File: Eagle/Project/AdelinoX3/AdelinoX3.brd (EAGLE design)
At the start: 47 x 53.3 mm, 80 parts, among them J1 DC-044-A, J2 YELLOW-8P-2.54, J3 YELLOW-6P-2.54, J4 YELLOW-8P-2.54, J5 YELLOW-8P-2.54, J6 4P-2.0, J7 YELLOW-2X3P-2.54, J8 4P-2.0, Q1 NCE3407A, Q2 CJ2305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

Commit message: Wip; use same parts as Seeeduino for SPS.
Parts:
- added L3, L4: 470R-2A, OPL_Ferrite_and_Magnetic_Bead:L0805
- added R30: 24K, Seeed-Resistor:R0603
- C2, C3: value 10uf -> 22uf; device Seeed-Capacitor:C0805 -> Seeed-Capacitor:C1206
- R1: value 100K 1/10W -> 100K
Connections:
- removed net SW_EN: R1.1, U2.6
- new net N$7: R1.2, R30.2, U2.6
- new net N$8: L3.1, Q1.2
- net GND: now also R30.1
- net SW_VCC_IN: now also L3.2, R1.1; no longer Q1.2, R1.2
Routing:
- net SW_EN: track 10.5 -> 0.00 mm, vias 2 -> 0
- net SW_VCC_IN: track 7.67 -> 3.56 mm

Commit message: Schematic changes to 0603 done.
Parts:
- added C22, C23: 10uf, Seeed-Capacitor:C0805
- added C24: 22uf, Seeed-Capacitor:C1206
- C6: value 10uf -> 22uf; device Seeed-Capacitor:C0805 -> OPL_Capacitor:C1206
- R28, R5: device Seeed-Resistor:R0402 -> Seeed-Resistor:R0603
- R4: value 10R 1/16W -> 10R; device Seeed-Resistor:R0402 -> Seeed-Resistor:R0603
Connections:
- new net N$10: C10.2, C22.2, C9.2, L2.2, L4.1, R7.2
- net +5V: now also C23.2, C24.2, L4.2; no longer C10.2, C9.2, L2.2, R7.2
- net GND: now also C22.1, C23.1, C24.1
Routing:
- net +5V: track 219.4 -> 208.7 mm
- net N$10: track 0.00 -> 9.04 mm
- net +3V3: track 111.6 -> 113.2 mm

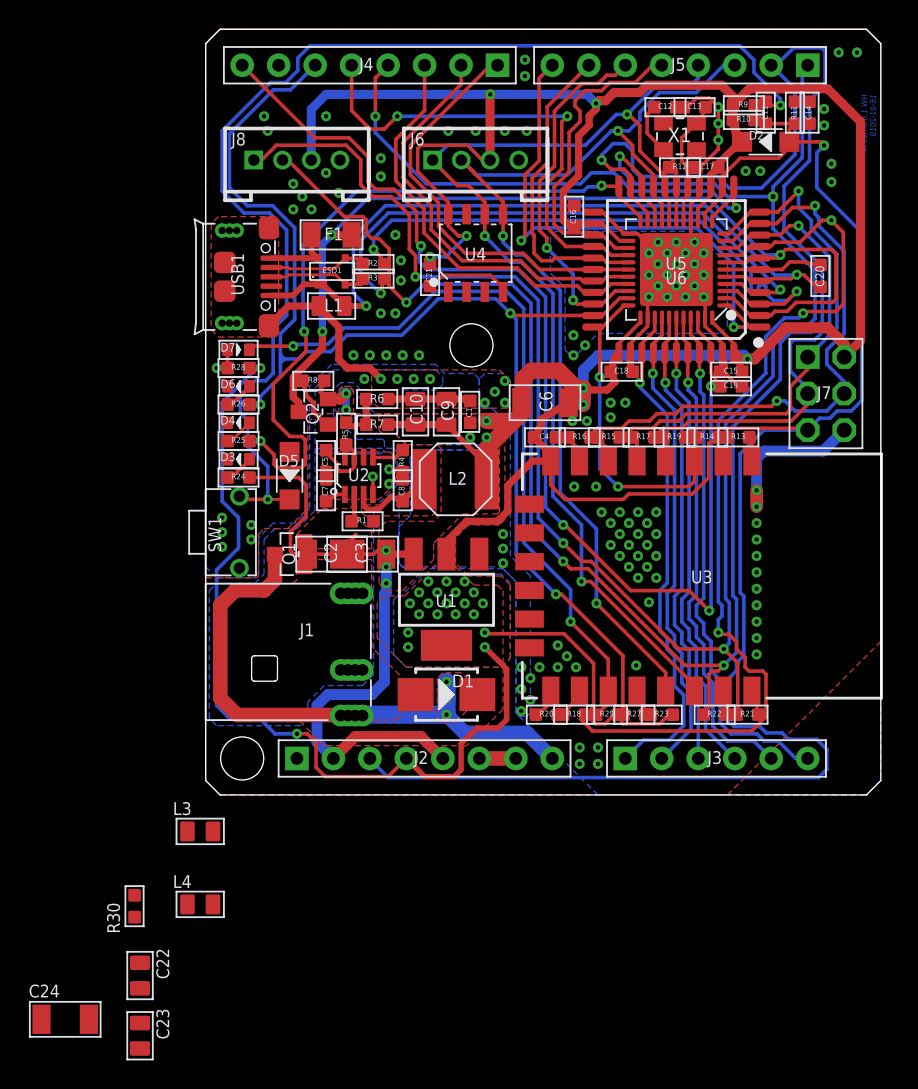
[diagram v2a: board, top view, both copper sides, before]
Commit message: First X3 routing finished.
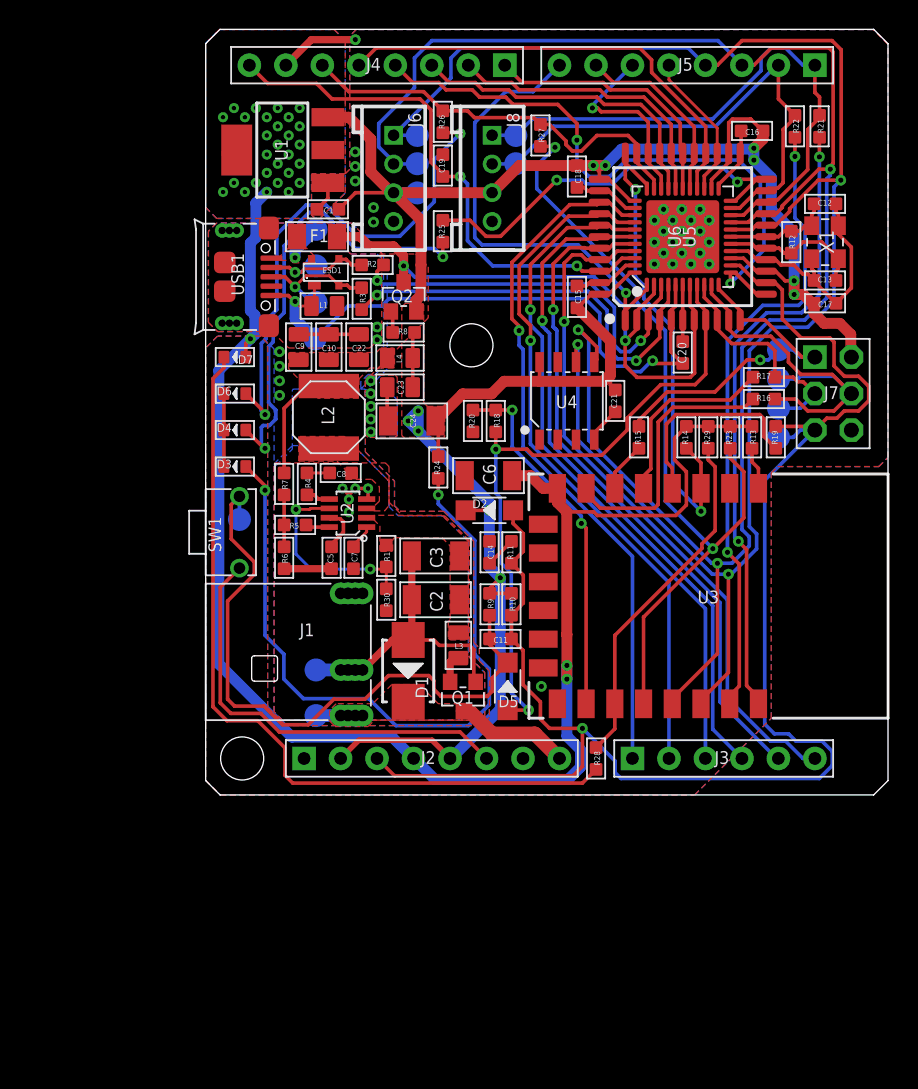
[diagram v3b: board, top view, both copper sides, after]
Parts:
- removed C4: 100nf, OPL_Capacitor:C0603
- added TP1, TP10, TP11, TP12, TP13, TP14, TP15, TP16, TP17, TP2, TP3, TP4, TP5, TP6, TP7, TP8, TP9: TPTP16R, testpad:TP16R
- R10, R20, R8, R9: value 100K 1/10W -> 100K
- R11, R13, R14, R23, R29: value 10K 1/10W -> 10K
- R12: value 1M 1/10W -> 1M
- R15, R16, R17, R21, R22, R24, R25, R26, R27: value 1K 1/10W -> 1K
- U1: value CJT1117-3.3-SOT223 -> CJT1117-3.3
- U3: device Seeed-OPL-2017-01-Sensor-camilo:ESP-12F -> Adelino-Misc:ESP-12F
- moved C23 48.6 mm to (13.5, 28.4), turned to 90 degrees
- moved C24 48.1 mm to (14.4, 26.0)
- moved C22 46.3 mm to (10.7, 31.2)
- moved R22 41.3 mm to (41.0, 46.5), turned to 180 degrees
- moved R21 41.3 mm to (42.7, 46.5), turned to 180 degrees
- moved C11 41.0 mm to (20.5, 10.9), turned to 270 degrees
- moved R27 40.8 mm to (23.3, 45.9), turned to 0 degrees
- moved L4 40.5 mm to (13.5, 30.4)
- moved R9 39.0 mm to (19.8, 13.3), turned to 0 degrees
- moved C14 37.9 mm to (19.8, 16.9), turned to 180 degrees
- moved R10 37.4 mm to (21.3, 13.3), turned to 180 degrees
- moved R28 36.9 mm to (27.2, 2.54), turned to 180 degrees
- moved R11 36.4 mm to (21.3, 16.9)
- moved U1 33.3 mm to (5.33, 44.9), turned to 90 degrees
- moved D2 32.1 mm to (19.7, 19.8)
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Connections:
- net N$10 renamed SW_F1
- net N$12 renamed GPIO12
- net N$14 renamed GPIO13
- net N$17 renamed TXD
- net N$18 renamed RXD
- net N$19 renamed GPIO14
- net N$20 renamed GPIO15
- net N$22 renamed RST
- net N$5 renamed GPIO16
- net N$6 renamed _ACT
- removed net N$1: ESD1.3, R2.1, USB1.2
- removed net N$2: ESD1.2, R3.1, USB1.3
- removed net N$4: D7.+, R28.2
- removed net N$9: ESD1.4, F1.1, USB1.1
- new net UD+: ESD1.2, R3.1, TP7.TP, USB1.3
- new net UD-: ESD1.3, R2.1, TP6.TP, USB1.2
- new net UVCC: ESD1.4, F1.1, TP5.TP, USB1.1
- new net _ESP: D7.-, R28.1
- net +3V3: now also D7.+, TP16.TP; no longer C4.2, R28.1
- net +5V: now also TP17.TP
- net AT_MISO: now also TP1.TP
- net AT_MOSI: now also TP4.TP
- net AT_SCK: now also TP2.TP
- net GND: now also TP10.TP; no longer C4.1
- net GPIO2_LED: now also R28.2; no longer D7.-
- net PIN_D0: now also TP12.TP
- net PIN_D1: now also TP13.TP
- net PIN_D2_SDA: now also TP14.TP
- net PIN_D3_SCL: now also TP15.TP
- net RESET: now also TP3.TP
- net RSTAT: now also TP11.TP
- net UGND: now also TP8.TP
- net VIN: now also TP9.TP
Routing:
- net PIN_D1: track 145.3 -> 36.1 mm, vias 4 -> 0
- net PIN_D0: track 129.5 -> 40.4 mm, vias 5 -> 0
- net PIN_D13: track 90.6 -> 28.8 mm, vias 3 -> 0
- net _ESP: track 0.00 -> 55.0 mm
- net BOOT_MODE: track 2.18 -> 55.7 mm, vias 0 -> 2
- net PIN_D2_SDA: track 73.7 -> 125.9 mm
- net _PWR: track 2.05 -> 49.4 mm, vias 0 -> 2
- net PIN_D3_SCL: track 76.2 -> 120.6 mm
- net +5V: track 208.7 -> 164.7 mm, vias 15 -> 11
- net PIN_AREF: track 81.5 -> 37.7 mm, vias 4 -> 2
- net RXD: track 1.73 -> 44.1 mm, vias 0 -> 2
- net TXD: track 1.75 -> 44.0 mm, vias 0 -> 2
- net RSTAT: track 81.2 -> 45.3 mm, vias 2 -> 0
- net GND: track 76.8 -> 111.2 mm, vias 137 -> 44
- net _D13: track 2.05 -> 35.5 mm, vias 0 -> 2
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- added copper zone on layer 1, net SW_F1
- added copper zone on layer 1, net UVCC
- removed copper zone on layer 16, net +5V
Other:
- board size 47 x 53.3 mm -> 47.5 x 53.3 mm
- board text added: "PWR"
- board text removed: "ECC 608"
- board text removed: "HW 1.0.0 Rev A 16-01-2019"
- board text removed: "I2C"
- board text removed: "ON"
- board text removed: "UART"

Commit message: Routing review in progress.
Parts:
- moved R18 1.65 mm to (18.5, 26.0)
- moved R20 1.46 mm to (20.1, 26.0)
- moved C23 0.13 mm to (13.7, 28.4)
- moved L4 0.13 mm to (13.7, 30.4)
- moved C24 0.13 mm to (14.5, 26.0)
- moved Q2 0.13 mm to (13.9, 34.7)
- moved R8 0.13 mm to (13.9, 32.2)
- moved C22 0.06 mm to (10.6, 31.2)
- moved C9 0.06 mm to (6.54, 31.2)
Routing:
- net AT_SS: track 45.9 -> 48.2 mm
- net +5V: track 164.7 -> 166.6 mm, vias 11 -> 10
- net N$8: track 1.76 -> 0.00 mm
- net GPIO15: track 25.3 -> 24.1 mm
- net UGND: track 44.6 -> 45.6 mm
- net D+: track 29.4 -> 30.4 mm
- net SW_VCC_OUT: track 0.92 -> 0.00 mm
- net D-: track 28.0 -> 28.8 mm
- net SW_VCC_IN: track 0.64 -> 0.00 mm
- net VUSB: track 44.0 -> 44.6 mm
- added copper zone on layer 1, net N$8

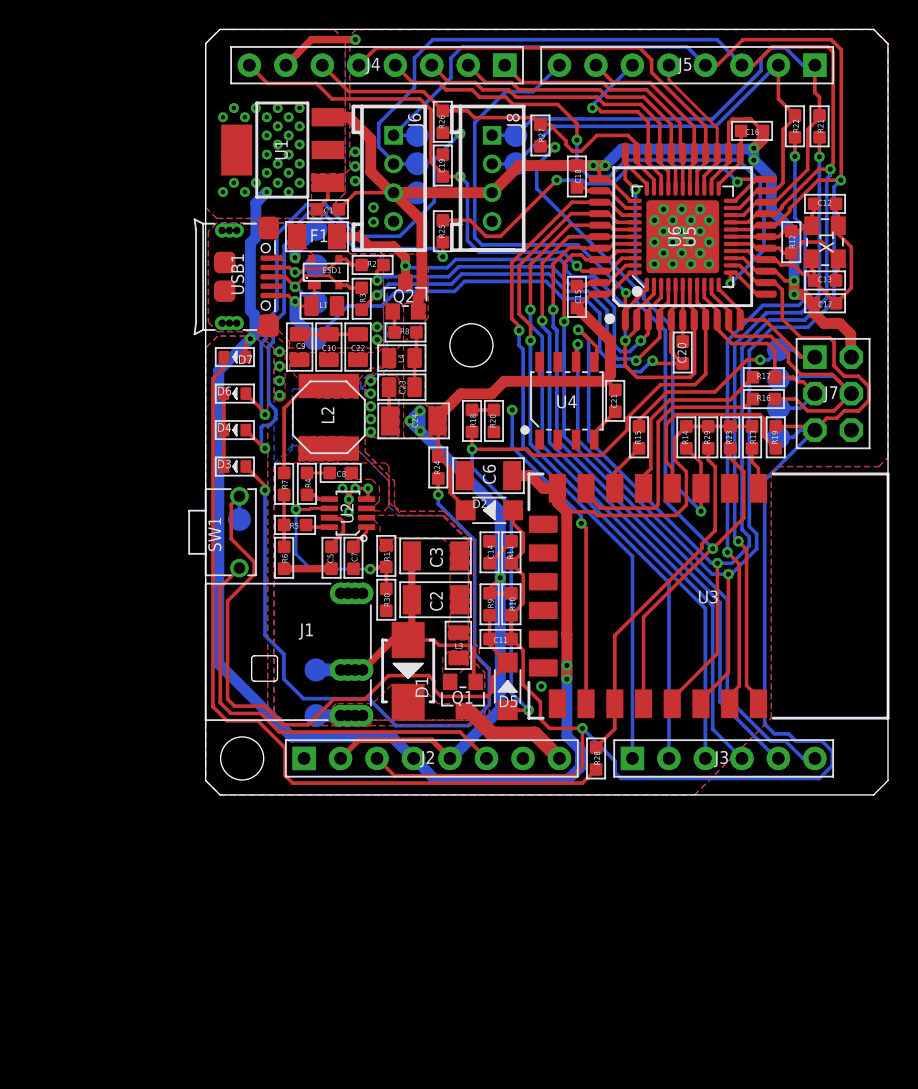
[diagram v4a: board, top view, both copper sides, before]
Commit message: Routing review finished.
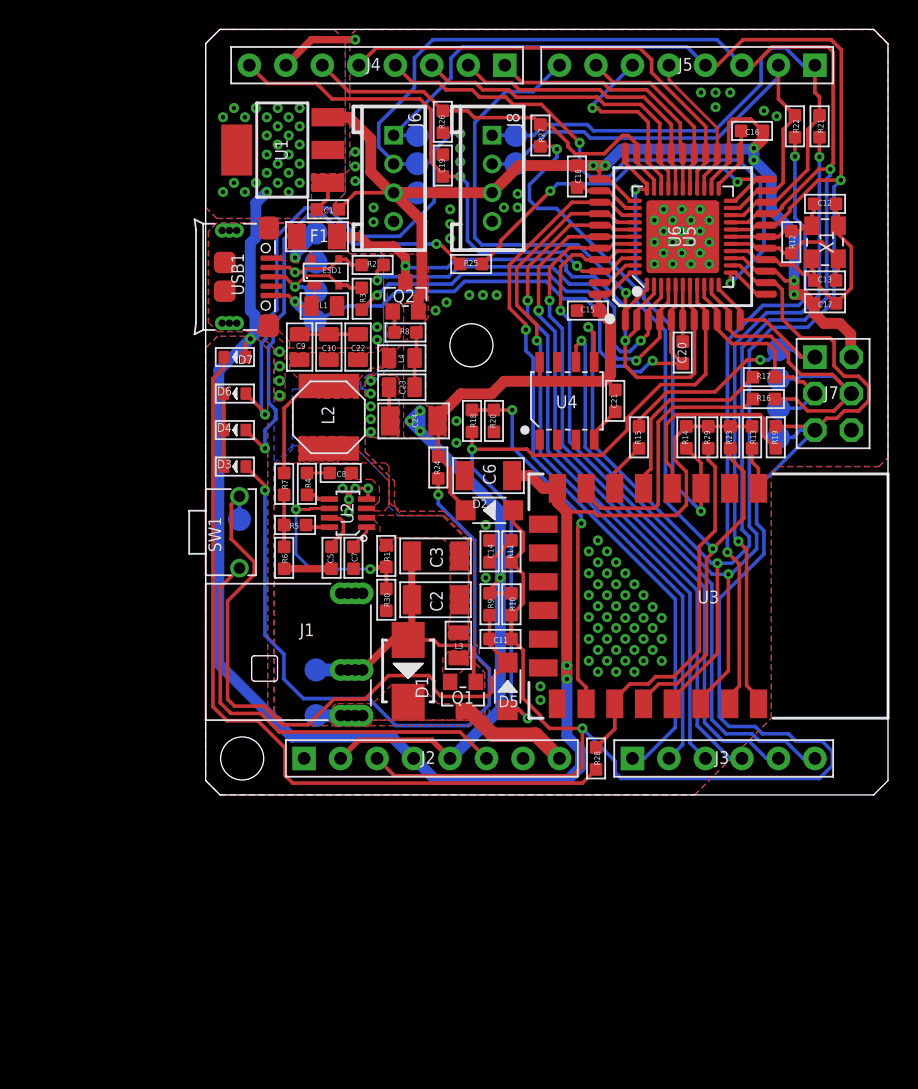
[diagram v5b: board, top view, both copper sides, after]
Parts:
- moved R25 3.02 mm to (18.5, 37.0), turned to 270 degrees
- moved TP8 1.27 mm to (7.62, 33.0)
- moved C15 1.22 mm to (26.6, 33.7), turned to 270 degrees
- moved TP7 0.76 mm to (7.68, 35.1)
- moved TP16 0.41 mm to (2.22, 44.9)
- moved TP6 0.25 mm to (7.68, 37.1)
- moved TP5 0.25 mm to (7.68, 39.1)
- moved C14 0.06 mm to (19.8, 17.0)
- moved R11 0.06 mm to (21.3, 17.0)
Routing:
- net RESET: track 112.1 -> 116.7 mm
- net PIN_A0: track 48.7 -> 51.8 mm
- net ACT_LED: track 28.7 -> 26.3 mm
- net GND: track 111.0 -> 108.6 mm, vias 44 -> 113
- net BOOT_MODE: track 55.7 -> 57.7 mm
- net ESP_EN: track 35.0 -> 33.0 mm
- net UGND: track 45.6 -> 43.6 mm
- net PIN_A5: track 48.3 -> 50.1 mm
- net PIN_A4: track 47.3 -> 49.0 mm
- net +5V: track 166.6 -> 164.9 mm
- net GPIO2_LED: track 24.5 -> 25.9 mm
- net GPIO15: track 24.1 -> 25.6 mm
- net PIN_A1: track 48.4 -> 49.3 mm
- net PIN_D0: track 40.4 -> 41.3 mm
- net PIN_D1: track 36.1 -> 37.0 mm
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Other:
- board text added: "AREF"
- board text removed: "ARF"

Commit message: Board review 1 (ground plane).
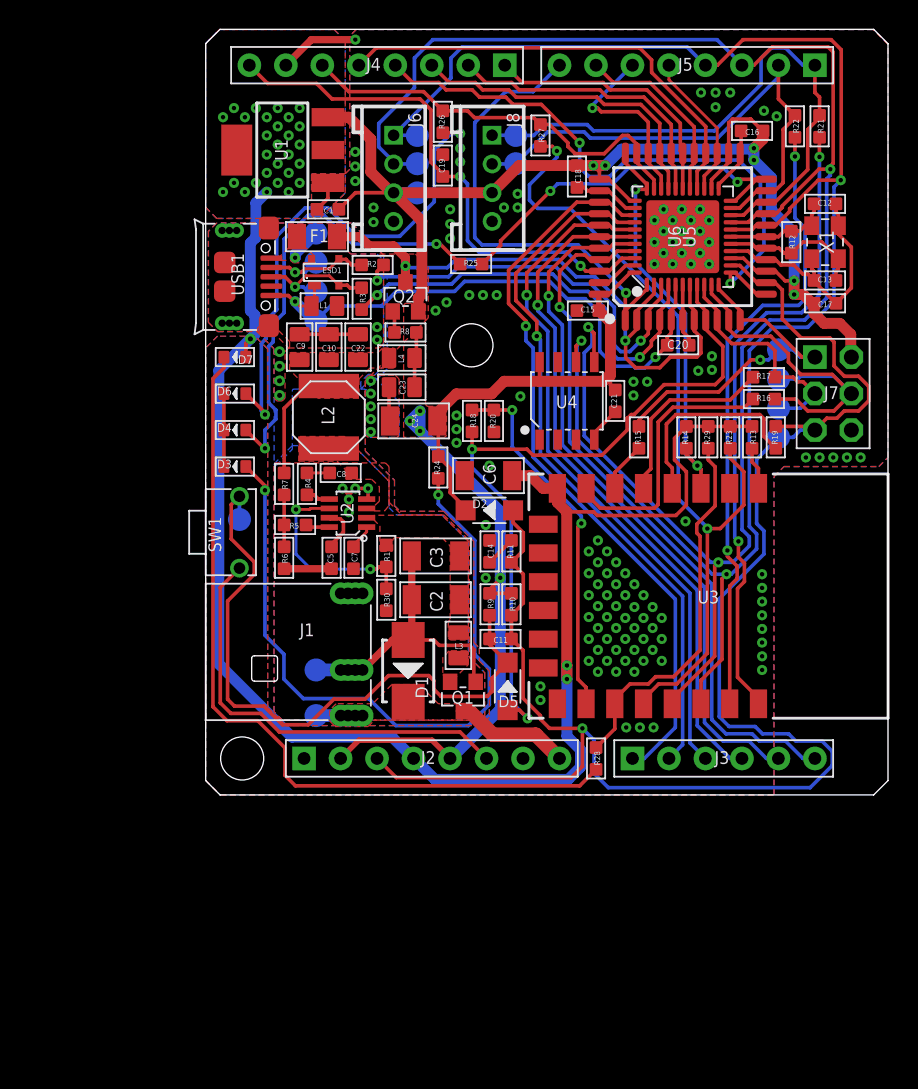
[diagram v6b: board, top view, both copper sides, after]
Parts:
- moved C20 0.60 mm to (32.9, 31.3), turned to 90 degrees
- moved TP8 0.06 mm to (7.68, 33.0)
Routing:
- net ESP_EN: track 33.0 -> 28.1 mm
- net UGND: track 43.6 -> 41.4 mm
- net AT_SS: track 48.9 -> 50.7 mm
- net VUSB: track 44.6 -> 43.3 mm
- net BOOT_MODE: track 57.7 -> 57.1 mm
- net GND: vias 113 -> 139

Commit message: Board review 2 (vias and silk).
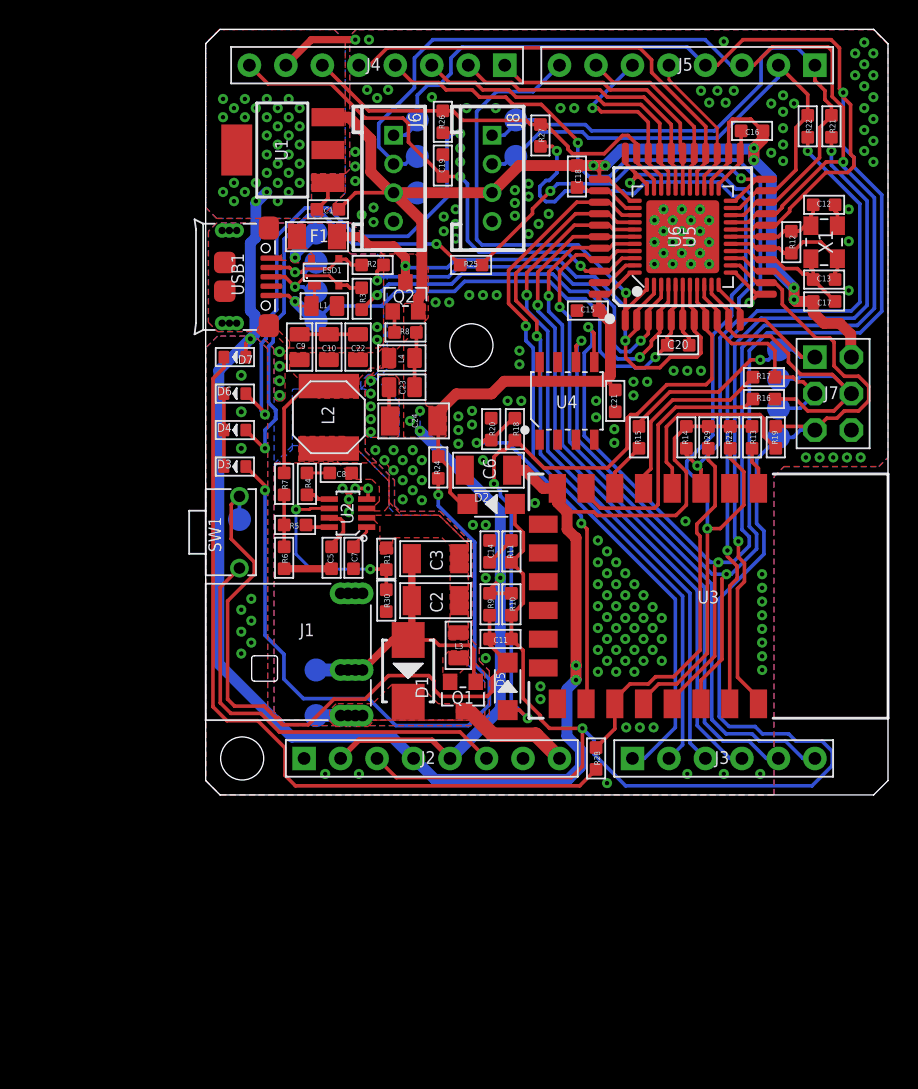
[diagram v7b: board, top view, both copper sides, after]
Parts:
- moved R18 3.04 mm to (21.5, 25.5)
- moved TP12 1.08 mm to (21.6, 47.0)
- moved TP15 1.08 mm to (14.7, 47.0)
- moved R22 0.89 mm to (41.9, 46.5)
- moved R21 0.83 mm to (43.6, 46.5)
- moved R20 0.60 mm to (19.9, 25.5), turned to 0 degrees
- moved TP13 0.51 mm to (21.6, 44.5)
- moved TP14 0.51 mm to (14.7, 44.5)
- moved D2 0.46 mm to (19.9, 20.3)
- moved C6 0.38 mm to (19.7, 22.6)
- moved C3 0.19 mm to (16.0, 16.4)
- moved R1 0.19 mm to (12.6, 16.4)
- moved C17 0.14 mm to (43.1, 34.4)
- moved C12 0.09 mm to (43.1, 41.1)
- moved C13 0.09 mm to (43.1, 35.9)
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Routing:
- net BOOT_MODE: track 57.1 -> 68.2 mm
- net PIN_D3_SCL: track 121.5 -> 132.2 mm
- net ESP_EN: track 28.1 -> 37.8 mm
- net GND: track 108.6 -> 99.4 mm, vias 139 -> 215
- net PIN_D2_SDA: track 126.1 -> 132.1 mm
- net RXD: track 43.9 -> 49.1 mm
- net TXD: track 44.4 -> 49.2 mm
- net AT_SS: track 50.7 -> 48.0 mm
- net +5V: track 165.1 -> 162.9 mm
- net PIN_AREF: track 37.7 -> 36.2 mm
- net PIN_D11: track 42.7 -> 43.9 mm
- net RESET: track 116.7 -> 115.6 mm
- net PIN_D0: track 41.3 -> 42.4 mm
- net +3V3: track 108.8 -> 109.5 mm, vias 31 -> 38
- net PIN_D1: track 37.0 -> 37.7 mm
- added copper zone on layer 16, net +5V
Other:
- board text added: "3"
- board text added: "A"
- board text added: "ATmega32U4"
- board text added: "Adelino X3 http://adelino.cc Product Validation Designed in Brazil"
- board text added: "C"
- board text added: "D"
- board text added: "E"
- board text added: "ECC 608"
- board text added: "I2C"
- board text added: "P"
- board text added: "R"
- board text added: "S"
- board text added: "T"
- board text added: "UART"
- board text added: "W"
- board text removed: "ACT"
- board text removed: "Adelino X2 http://adelino.cc Product Validation Designed in Brazil"
- board text removed: "D13"
- board text removed: "ESP"
- board text removed: "PWR"

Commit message: Fix polygon instead of wire on +5V root.
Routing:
- net +5V: track 162.9 -> 166.3 mm
- removed copper zone on layer 16, net +5V
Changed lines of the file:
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@@
 <wire x1="39.6745" y1="36.462" x2="39.0105" y2="36.462" width="0.254" layer="1"/>
 <wire x1="40.8305" y1="35.306" x2="39.6745" y2="36.462" width="0.254" layer="1"/>
-<polygon width="0.762" layer="16" rank="0">
-<vertex x="14.9225" y="25.3365"/>
-<vertex x="14.224" y="26.035"/>
-<vertex x="14.9225" y="26.7335"/>
-</polygon>
+<wire x1="14.9225" y1="25.3365" x2="14.9225" y2="26.7335" width="0.762" layer="16"/>
+<wire x1="14.9225" y1="26.7335" x2="14.224" y2="26.035" width="0.762" layer="16"/>
+<wire x1="14.224" y1="26.035" x2="14.9225" y2="25.3365" width="0.762" layer="16"/>
 </signal>
 <signal name="N$3">
